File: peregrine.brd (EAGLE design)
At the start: 55.9 x 55.9 mm, 77 parts, among them Q1 BSS123, Q10 BSS123, Q11 BSS123, Q2 BSS123, U1 ITG-3200, U2 ADXL345, U5 ATMEGA32U4-XUAU, X2 USB-MICROB, Y1 16MHz KX-7

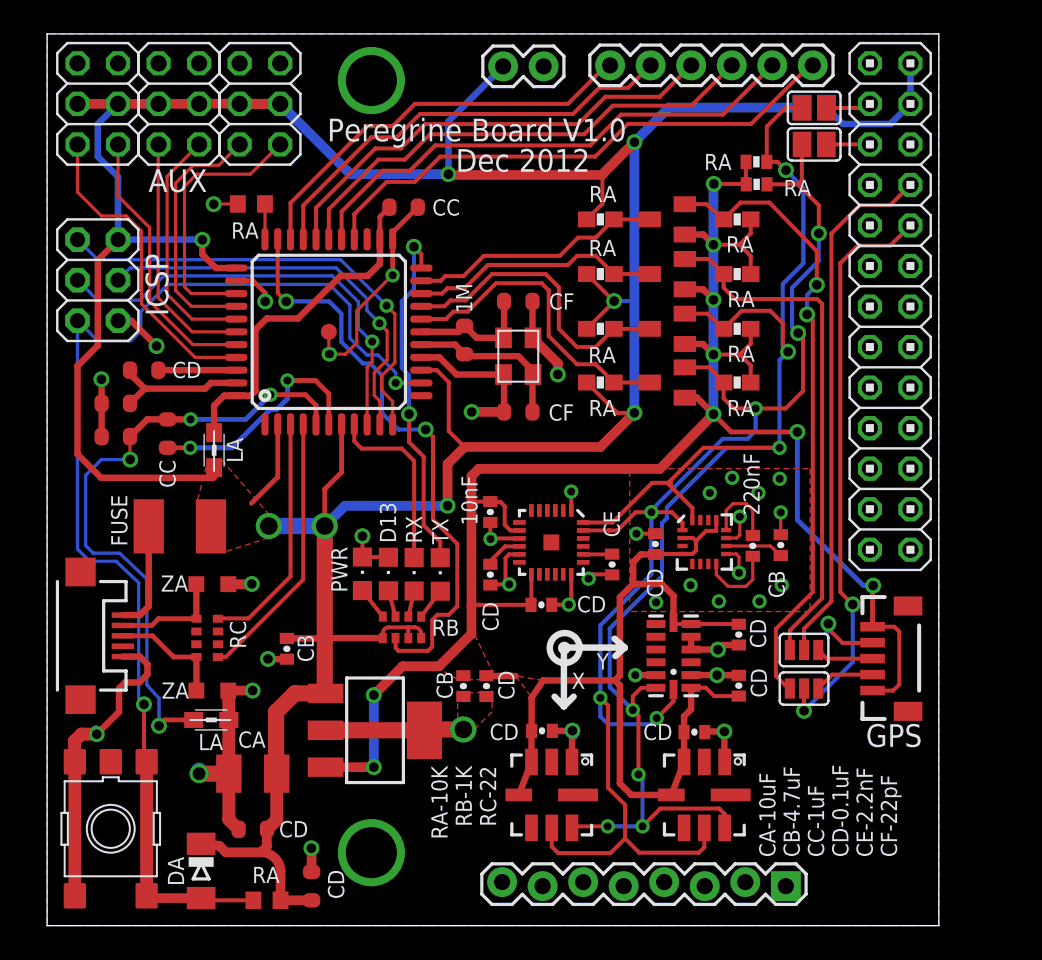
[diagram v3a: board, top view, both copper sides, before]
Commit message: Made room in layout for cutout
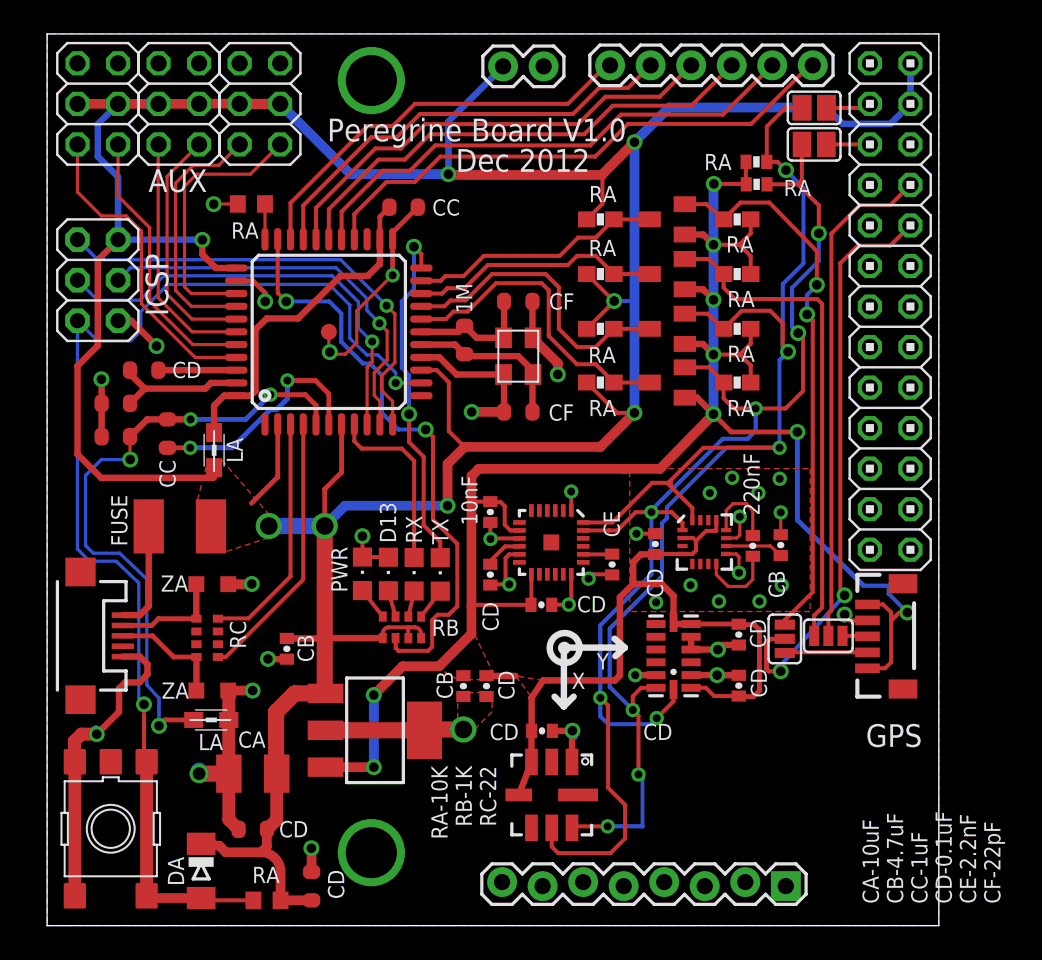
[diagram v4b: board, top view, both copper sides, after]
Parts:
- removed C13: 0.1uF, SparkFun:0402-CAP
- removed U$3: BMP085, SparkFun:BMP085
- moved SJ7 3.34 mm to (46.2, 18.0), turned to 90 degrees
- moved SJ8 1.76 mm to (49.0, 18.2)
- moved GPS 1.43 mm to (51.4, 16.1)
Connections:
- net 3V3: no longer C13.1, U$3.3, U$3.4
- net GND: no longer C13.2, U$3.1
- net SCL3V3: no longer U$3.6
- net SDA3V3: no longer U$3.7
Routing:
- net SCL3V3: track 88.8 -> 82.1 mm
- net SDA3V3: track 96.0 -> 89.4 mm, vias 7 -> 6
- net 3V3: track 175.7 -> 169.5 mm
- net AT_TX3V3: track 39.5 -> 34.9 mm
- net GND: track 129.1 -> 124.8 mm, vias 41 -> 39
- net GPIO15(RXD): track 36.4 -> 39.6 mm
- net GPS-INPUT: track 3.63 -> 1.58 mm
- net GPIO14(TXD): track 33.0 -> 31.5 mm
- net AT_RX3V3: track 32.8 -> 31.3 mm
- net GPS-OUTPUT: track 3.77 -> 5.20 mm

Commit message: Added notch for RCA connector
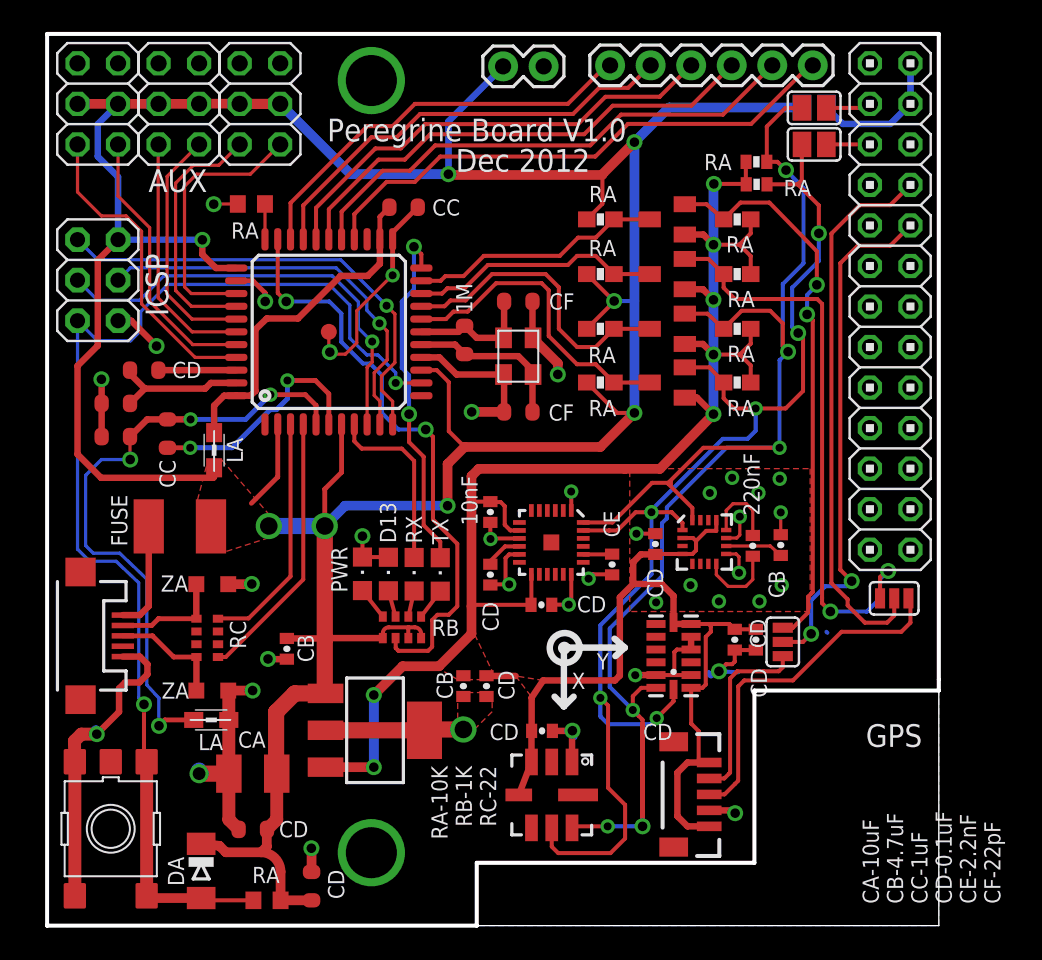
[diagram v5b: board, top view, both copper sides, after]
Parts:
- removed JTAG: (no value), SparkFun:1X08_LOCK
- moved GPS 11.5 mm to (41.5, 10.2), turned to 270 degrees
- moved SJ8 4.75 mm to (53.1, 20.5)
- moved C2 3.07 mm to (44.4, 17.9), turned to 270 degrees
- moved C1 0.41 mm to (43.1, 17.9)
- moved SJ7 0.23 mm to (46.1, 17.8)
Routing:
- net 3V3: track 169.5 -> 146.6 mm, vias 9 -> 7
- net GPS-INPUT: track 1.58 -> 22.1 mm
- net GPIO15(RXD): track 39.6 -> 32.7 mm
- net SDA3V3: track 89.4 -> 95.9 mm, vias 6 -> 7
- net GPS-OUTPUT: track 5.20 -> 11.7 mm
- net AT_RX3V3: track 31.3 -> 37.1 mm, vias 0 -> 2
- net GPIO14(TXD): track 31.5 -> 34.6 mm
- net GND: track 124.8 -> 127.2 mm, vias 39 -> 38
- net AT_TX3V3: track 34.9 -> 35.5 mm
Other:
- outline, holes or cut-outs redrawn

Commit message: Changed outline, removed unused parts, via stops
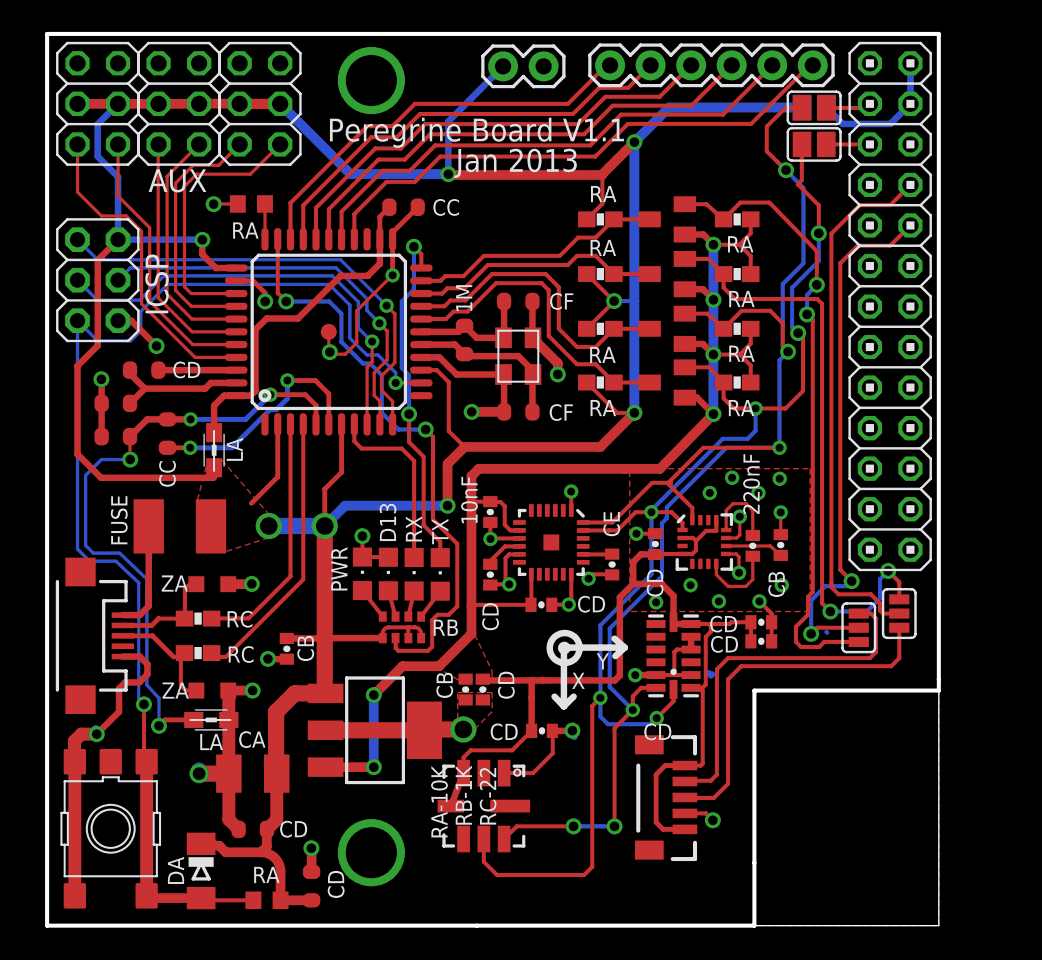
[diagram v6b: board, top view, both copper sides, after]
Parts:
- removed C10: 0.1uF, SparkFun:0402-CAP
- removed C12: 4.7uF, SparkFun:0402-CAP
- removed R1, R2: 4.7K, SparkFun:0402-RES
- removed RN3: 22R, resistor-dil:CAY16
- added C13: 0.1uF, SparkFun:0402-CAP
- added C15: 4.7uF, SparkFun:0402-CAP
- added R13, R3: 22, SparkFun:0603-RES
- moved SJ7 4.84 mm to (50.9, 18.7), turned to 270 degrees
- moved U$4 4.31 mm to (27.4, 7.49)
- moved C1 1.67 mm to (44.8, 17.8), turned to 0 degrees
- moved GPS 1.54 mm to (40.0, 10.0)
- moved C2 1.14 mm to (44.8, 19.0), turned to 0 degrees
- moved SJ8 1.00 mm to (53.4, 19.6), turned to 90 degrees
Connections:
- net 3V3: now also C13.1, C15.1; no longer C10.1, C12.1, R1.2, R2.2
- net D+: now also R13.2; no longer RN3.8
- net D-: now also R3.2; no longer RN3.5
- net GND: now also C13.2, C15.2; no longer C10.2, C12.2
- net RD+: now also R13.1; no longer RN3.1
- net RD-: now also R3.1; no longer RN3.4
- net SCL3V3: no longer R2.1
- net SDA3V3: no longer R1.1
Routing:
- net GPS-OUTPUT: track 11.7 -> 22.5 mm
- net AT_TX3V3: track 35.5 -> 39.9 mm
- net SDA3V3: track 95.9 -> 92.0 mm, vias 7 -> 6
- net SCL3V3: track 82.1 -> 84.0 mm
- net GND: track 127.2 -> 128.7 mm, vias 38 -> 37
- net GPIO15(RXD): track 32.7 -> 33.9 mm
- net GPS-INPUT: track 22.1 -> 22.8 mm
- net GPIO14(TXD): track 34.6 -> 33.9 mm
- net 3V3: track 146.6 -> 146.5 mm, vias 7 -> 6
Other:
- outline, holes or cut-outs redrawn
- board text added: "Jan 2013"
- board text added: "Peregrine Board V1.1"
- board text removed: "CA-10uF CB-4.7uF CC-1uF CD-0.1uF CE-2.2nF CF-22pF"
- board text removed: "Dec 2012"
- board text removed: "GPS"
- board text removed: "Peregrine Board V1.0"

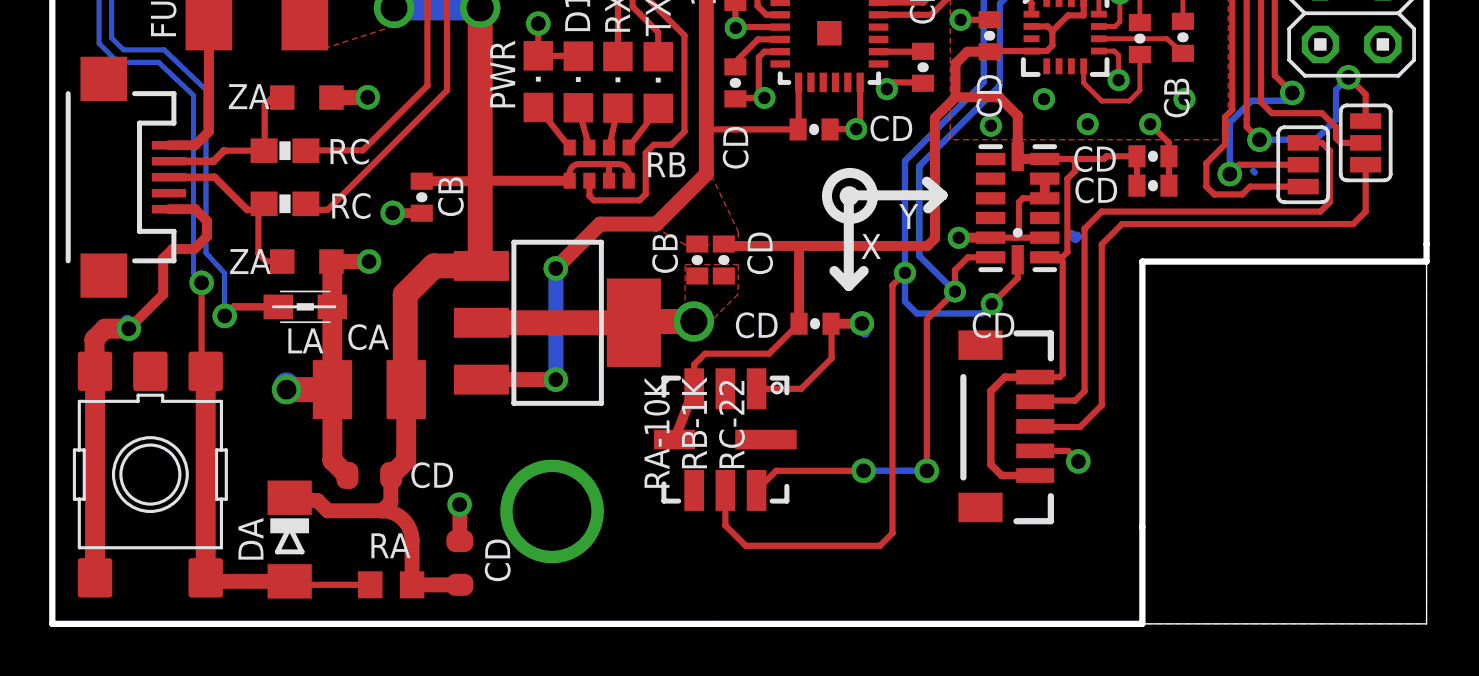
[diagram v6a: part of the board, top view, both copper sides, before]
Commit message: Moved outline a bit, added gerbers
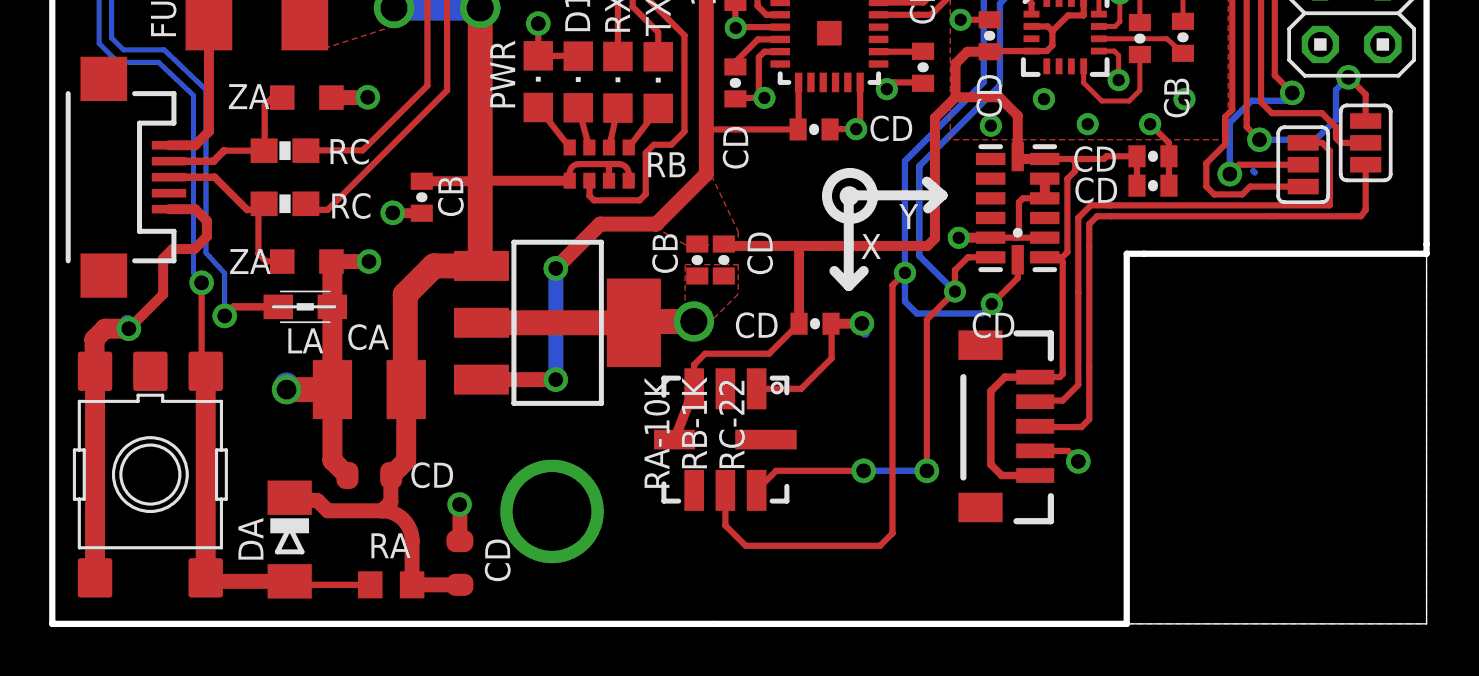
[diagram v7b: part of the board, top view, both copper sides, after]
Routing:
- net GPS-INPUT: track 22.8 -> 23.6 mm
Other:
- outline, holes or cut-outs redrawn
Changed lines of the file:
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@@
 <board>
 <plain>
-<wire x1="55.88" y1="0" x2="55.88" y2="15.4305" width="0" layer="20"/>
+<wire x1="55.88" y1="0" x2="55.88" y2="15.0495" width="0" layer="20"/>
+<wire x1="55.88" y1="15.0495" x2="55.88" y2="15.4305" width="0" layer="20"/>
 <wire x1="55.88" y1="15.4305" x2="55.88" y2="55.88" width="0" layer="20"/>
 <wire x1="55.88" y1="55.88" x2="0" y2="55.88" width="0" layer="20"/>
 <wire x1="0" y1="55.88" x2="0" y2="0" width="0" layer="20"/>
-<wire x1="0" y1="0" x2="44.323" y2="0" width="0" layer="20"/>
+<wire x1="0" y1="0" x2="43.688" y2="0" width="0" layer="20"/>
 <text x="25.146" y="23.9014" size="1.016" layer="25" font="vector" ratio="12" rot="R90">TX</text>
 <text x="23.495" y="23.9522" size="1.016" layer="25" font="vector" ratio="12" rot="R90">RX</text>
 <text x="18.8214" y="20.8788" size="1.016" layer="25" font="vector" ratio="12" rot="R90">PWR</text>
 <text x="21.8694" y="23.9776" size="1.016" layer="25" font="vector" ratio="12" rot="R90">D13</text>
-<wire x1="44.323" y1="0" x2="55.88" y2="0" width="0" layer="20"/>
+<wire x1="43.688" y1="0" x2="55.88" y2="0" width="0" layer="20"/>
 <wire x1="32.385" y1="17.4244" x2="32.385" y2="13.7414" width="0.4064" layer="25"/>
 <wire x1="32.385" y1="13.7414" x2="31.8008" y2="14.351" width="0.4064" layer="25"/>
@@
 <text x="7.5946" y="38.2016" size="1.4224" layer="25" font="vector" ratio="12" rot="R90">ICSP</text>
 <wire x1="0" y1="0" x2="26.924" y2="0" width="0.254" layer="20"/>
-<wire x1="26.924" y1="0" x2="44.323" y2="0" width="0.254" layer="20"/>
-<wire x1="44.323" y1="0" x2="44.323" y2="3.937" width="0.254" layer="20"/>
-<wire x1="44.323" y1="3.937" x2="44.323" y2="14.732" width="0.254" layer="20"/>
-<wire x1="44.323" y1="14.732" x2="55.88" y2="14.732" width="0.254" layer="20"/>
-<wire x1="55.88" y1="14.732" x2="55.88" y2="15.4305" width="0.254" layer="20"/>
+<wire x1="26.924" y1="0" x2="43.688" y2="0" width="0.254" layer="20"/>
+<wire x1="43.688" y1="0" x2="43.688" y2="15.0495" width="0.254" layer="20"/>
+<wire x1="43.688" y1="15.0495" x2="44.3865" y2="15.0495" width="0.254" layer="20"/>
+<wire x1="44.3865" y1="15.0495" x2="55.88" y2="15.0495" width="0.254" layer="20"/>
+<wire x1="55.88" y1="15.0495" x2="55.88" y2="15.4305" width="0.254" layer="20"/>
 <wire x1="55.88" y1="15.4305" x2="55.88" y2="55.88" width="0.254" layer="20"/>
 <wire x1="55.88" y1="55.88" x2="0" y2="55.88" width="0.254" layer="20"/>
@@
 <wire x1="32.9184" y1="11.9634" x2="33.0454" y2="11.8364" width="0.4064" layer="16"/>
 <wire x1="32.893" y1="12.192" x2="32.9184" y2="12.2174" width="0.4064" layer="1"/>
-<wire x1="41.4147" y1="15.8242" x2="41.6052" y2="15.6972" width="0.4064" layer="16"/>
-<wire x1="41.6052" y1="15.6972" x2="41.656" y2="15.748" width="0.4064" layer="16"/>
 <wire x1="40.3557" y1="17.3037" x2="40.3557" y2="18.1037" width="0.4064" layer="1"/>
 <wire x1="27.7749" y1="25.2707" x2="27.7749" y2="24.3459" width="0.254" layer="1"/>
@@
 <contactref element="SJ8" pad="1"/>
 <contactref element="GPS" pad="3"/>
-<wire x1="53.4035" y1="18.669" x2="53.4035" y2="16.764" width="0.254" layer="1"/>
-<wire x1="53.4035" y1="16.764" x2="52.8955" y2="16.256" width="0.254" layer="1"/>
-<wire x1="52.8955" y1="16.256" x2="43.4975" y2="16.256" width="0.254" layer="1"/>
-<wire x1="43.4975" y1="16.256" x2="42.672" y2="15.4305" width="0.254" layer="1"/>
-<wire x1="42.672" y1="15.4305" x2="42.672" y2="8.89" width="0.254" layer="1"/>
-<wire x1="42.672" y1="8.89" x2="41.783" y2="8.001" width="0.254" layer="1"/>
 <wire x1="41.783" y1="8.001" x2="39.9989" y2="8.001" width="0.254" layer="1"/>
 <wire x1="39.9989" y1="8.001" x2="39.9669" y2="8.033" width="0.254" layer="1"/>
+<wire x1="53.4035" y1="18.669" x2="53.4035" y2="16.891" width="0.254" layer="1"/>
+<wire x1="53.4035" y1="16.891" x2="53.4035" y2="16.8275" width="0.254" layer="1"/>
+<wire x1="53.4035" y1="16.8275" x2="53.213" y2="16.5735" width="0.254" layer="1"/>
+<wire x1="53.213" y1="16.5735" x2="49.5935" y2="16.5735" width="0.254" layer="1"/>
+<wire x1="49.5935" y1="16.5735" x2="43.053" y2="16.5735" width="0.254" layer="1"/>
+<wire x1="42.164" y1="8.3185" x2="42.164" y2="10.414" width="0.254" layer="1"/>
+<wire x1="41.783" y1="8.001" x2="41.8465" y2="8.001" width="0.254" layer="1"/>
+<wire x1="41.8465" y1="8.001" x2="42.164" y2="8.3185" width="0.254" layer="1"/>
+<wire x1="42.164" y1="10.414" x2="42.164" y2="15.367" width="0.254" layer="1"/>
+<wire x1="42.164" y1="15.367" x2="42.164" y2="16.256" width="0.254" layer="1"/>
+<wire x1="42.164" y1="16.256" x2="42.4815" y2="16.5735" width="0.254" layer="1"/>
+<wire x1="42.4815" y1="16.5735" x2="43.053" y2="16.5735" width="0.254" layer="1"/>
 </signal>
 <signal name="GPS-OUTPUT">
@@
 <wire x1="50.8635" y1="19.558" x2="51.6255" y2="19.558" width="0.254" layer="1"/>
 <wire x1="51.6255" y1="19.558" x2="51.943" y2="19.2405" width="0.254" layer="1"/>
-<wire x1="51.943" y1="19.2405" x2="51.943" y2="17.145" width="0.254" layer="1"/>
-<wire x1="51.943" y1="17.145" x2="51.562" y2="16.764" width="0.254" layer="1"/>
-<wire x1="51.562" y1="16.764" x2="42.672" y2="16.764" width="0.254" layer="1"/>
-<wire x1="42.672" y1="16.764" x2="41.9735" y2="16.0655" width="0.254" layer="1"/>
-<wire x1="41.9735" y1="16.0655" x2="41.9735" y2="9.4615" width="0.254" layer="1"/>
-<wire x1="41.9735" y1="9.4615" x2="41.5925" y2="9.0805" width="0.254" layer="1"/>
-<wire x1="41.5925" y1="9.0805" x2="40.0144" y2="9.0805" width="0.254" layer="1"/>
+<wire x1="51.943" y1="19.2405" x2="51.943" y2="17.018" width="0.254" layer="1"/>
+<wire x1="41.0845" y1="9.0805" x2="40.0144" y2="9.0805" width="0.254" layer="1"/>
 <wire x1="40.0144" y1="9.0805" x2="39.9669" y2="9.033" width="0.254" layer="1"/>
+<wire x1="51.943" y1="17.018" x2="43.053" y2="17.018" width="0.254" layer="1"/>
+<wire x1="43.053" y1="17.018" x2="42.926" y2="17.018" width="0.254" layer="1"/>
+<wire x1="42.926" y1="17.018" x2="42.2275" y2="17.018" width="0.254" layer="1"/>
+<wire x1="42.2275" y1="17.018" x2="41.7195" y2="16.51" width="0.254" layer="1"/>
+<wire x1="41.7195" y1="16.51" x2="41.7195" y2="13.462" width="0.254" layer="1"/>
+<wire x1="41.7195" y1="13.462" x2="41.7195" y2="9.7155" width="0.254" layer="1"/>
+<wire x1="41.7195" y1="9.7155" x2="41.0845" y2="9.0805" width="0.254" layer="1"/>
 </signal>
 <signal name="GPIO18(PCM_CLK)">
